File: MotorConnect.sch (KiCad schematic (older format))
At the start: 1 part, among them J19 Stepper

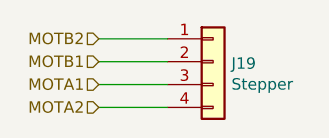
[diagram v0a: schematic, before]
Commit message: Added pul-ups on the UART ports and series resistors for protection.
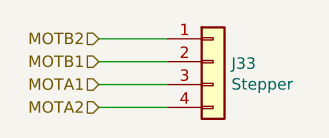
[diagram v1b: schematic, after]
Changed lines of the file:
@@
 AR Path="/5AC337B6/5AD1664A/5AD1665E/5AD04DCC" Ref="J30"  Part="1"
 AR Path="/5AC337B6/5AD9F95A/5AD4C411/5AD04DCC" Ref="J33"  Part="1"
-F 0 "J19" H 4480 2692 50  0000 L CNN
+F 0 "J33" H 4480 2692 50  0000 L CNN
 F 1 "Stepper" H 4480 2601 50  0000 L CNN
 F 2 "kicad-molex-sl-footprints:Molex-SL-4POS" H 4400 2700 50  0001 C CNN
